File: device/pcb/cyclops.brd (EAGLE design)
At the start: 124.5 x 79.9 mm, 201 parts, among them Q1 NDS351AN, Q2 NDS351AN, Q3 NDS351AN, Q4 IRF510, U1 MCP4921, U10 LT1880, U11 ZXTD, U12 DG9421, U13 THS4281, U14 ZXTD, U16 OPA1664, U2 LT1764A, U3 BD00FC0WEFJ, U4 LTM8020, U5 LT1931, U6 TPS72325, U7 TLV3701, U75 TXB0104RGYR, U8 LT1711, U9 ADR03

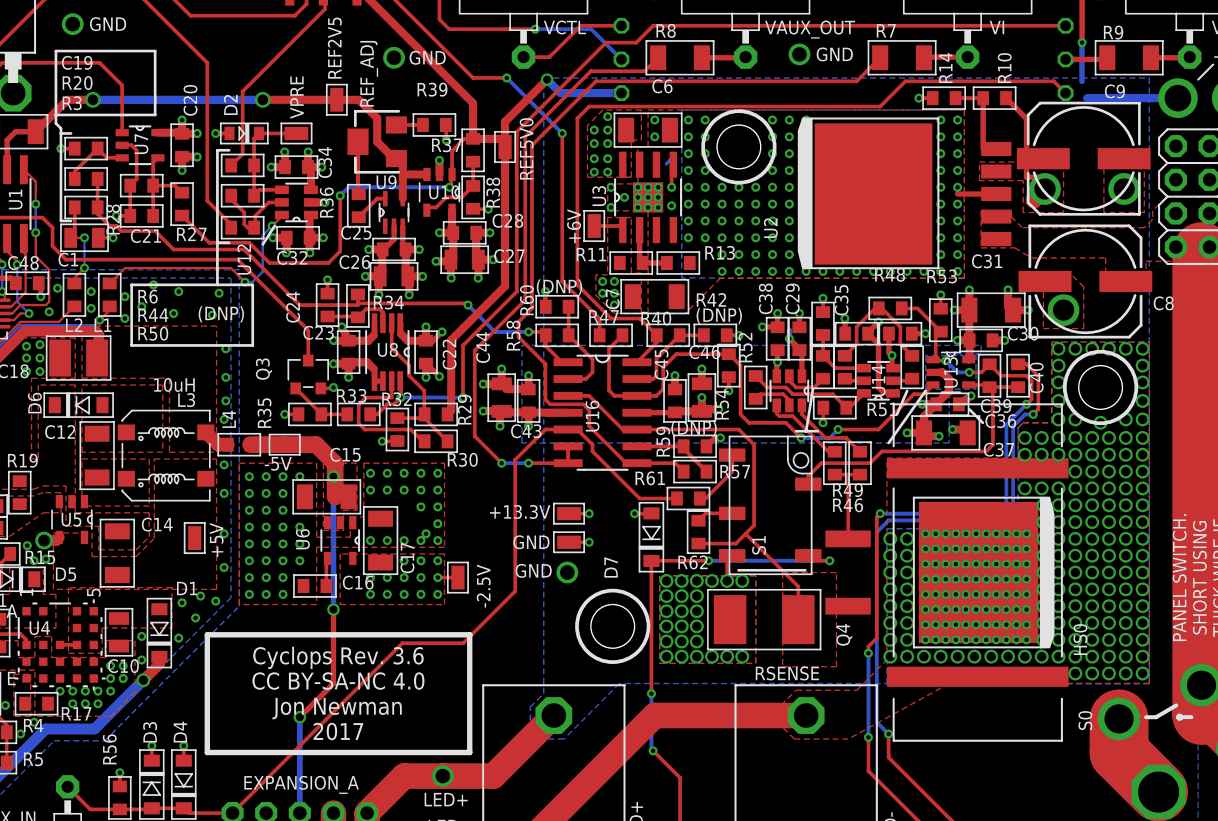
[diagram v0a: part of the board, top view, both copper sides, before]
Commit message: Ready for 3.6 production
- These designs are up to date for 3.6 production
- I need to create an assembly manual before moving forward
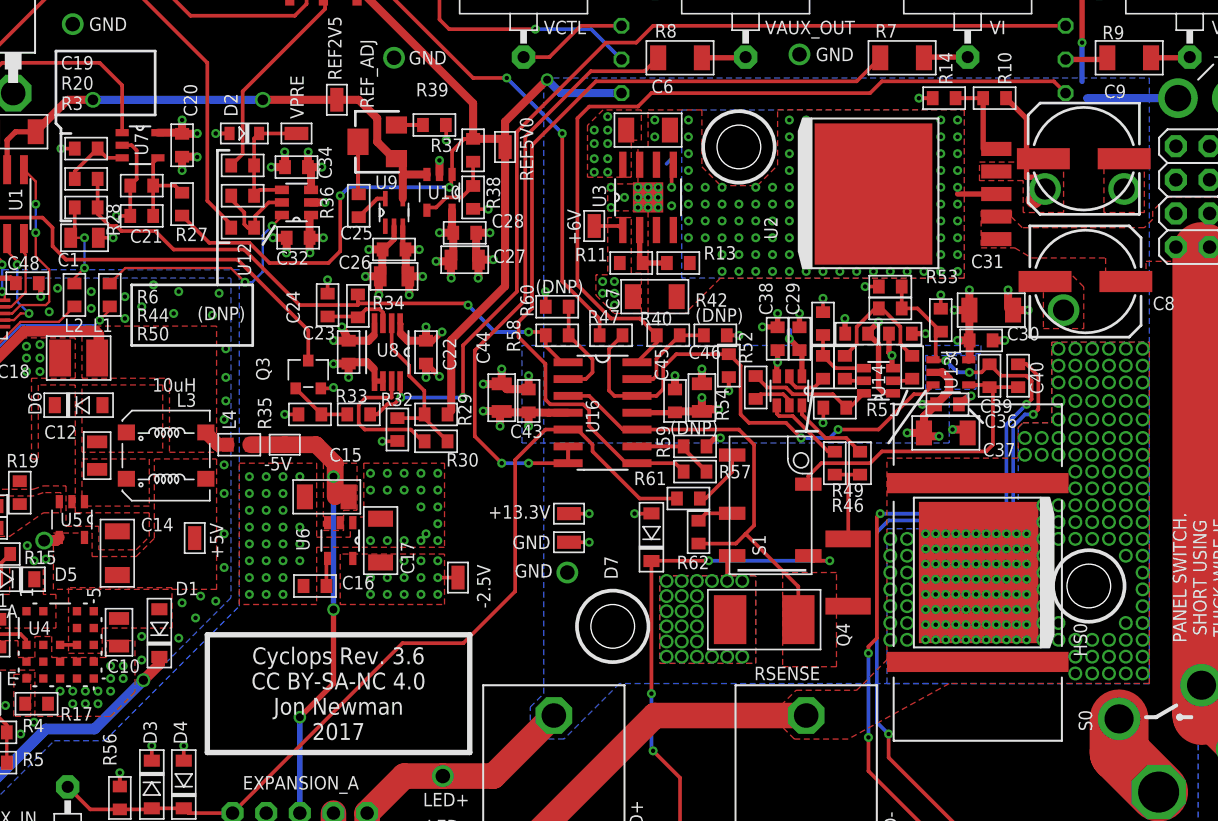
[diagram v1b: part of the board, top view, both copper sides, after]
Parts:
- added C41: 470pF, cyclops:0603
- C12: device cyclops:1206 -> jonnew:0805
- R48: value 0 -> 200
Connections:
- net GND: now also C41.2
- net N$13: now also C41.1
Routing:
- net N$13: track 66.7 -> 68.4 mm
- net GND: track 113.7 -> 114.7 mm, vias 415 -> 407
- net LED-: vias 233 -> 210

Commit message: Fixed erros found in pre-production check by Filipe.
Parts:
- R36: value 470 -> 470k
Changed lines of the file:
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@@
 <?xml version="1.0" encoding="utf-8"?>
 <!DOCTYPE eagle SYSTEM "eagle.dtd">
-<eagle version="6.5.0">
+<eagle version="6.6.0">
 <drawing>
 <settings>
@@
 <attribute name="VALUE" x="62.865" y="53.474" size="1.016" layer="27" font="vector" ratio="18"/>
 </element>
-<element name="R36" library="cyclops" package="0603" value="470" x="52.832" y="56.268" smashed="yes" rot="R270">
+<element name="R36" library="cyclops" package="0603" value="470k" x="52.832" y="56.268" smashed="yes" rot="R270">
 <attribute name="MN" value="Panasonic" x="52.832" y="53.728" size="1.778" layer="27" rot="R270" display="off"/>
 <attribute name="DK" value="PxxxxHTR-ND" x="52.832" y="53.728" size="1.778" layer="27" rot="R270" display="off"/>

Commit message: Fixed erros found in pre-production check by Filipe.
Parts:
- U12: value DG9421 -> ADG1201
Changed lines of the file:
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@@
 <attribute name="MPN" value="ERJ-3EKFxxxxV" x="52.832" y="53.728" size="1.778" layer="27" rot="R270" display="off"/>
 <attribute name="NAME" x="50.927" y="55.252" size="1.016" layer="25" font="vector" ratio="18" rot="R90"/>
-<attribute name="VALUE" x="52.07" y="55.125" size="1.016" layer="27" font="vector" ratio="18" rot="R90"/>
+<attribute name="VALUE" x="52.07" y="54.998" size="1.016" layer="27" font="vector" ratio="18" rot="R90"/>
 </element>
 <element name="R39" library="cyclops" package="0603" value="1k" x="58.547" y="62.364" smashed="yes" rot="R180">
@@
 <element name="C34" library="cyclops" package="0603" value="0.1uF" x="48.133" y="59.182" smashed="yes" rot="R180">
 <attribute name="NAME" x="50.292" y="58.293" size="1.016" layer="25" font="vector" ratio="18" rot="R270" align="center-right"/>
-<attribute name="VALUE" x="51.308" y="58.293" size="1.016" layer="27" font="vector" ratio="18" rot="R90" align="center-left"/>
+<attribute name="VALUE" x="51.308" y="58.42" size="1.016" layer="27" font="vector" ratio="18" rot="R90" align="center-left"/>
 </element>
 <element name="C32" library="cyclops" package="0603" value="0.1uF" x="48.26" y="53.848" smashed="yes" rot="R180">
@@
 <attribute name="VALUE" x="56.709" y="47.169" size="1.016" layer="27" font="vector" ratio="18" rot="SR0"/>
 </element>
-<element name="U12" library="jonnew" package="SOT23-6" value="DG9421" x="48.133" y="56.515" smashed="yes" rot="R90">
+<element name="U12" library="jonnew" package="SOT23-6" value="ADG1201" x="48.133" y="56.515" smashed="yes" rot="R90">
 <attribute name="VALUE" x="45.085" y="53.594" size="1.016" layer="27" font="vector" ratio="18" rot="R270"/>
 <attribute name="NAME" x="43.688" y="53.467" size="1.016" layer="25" font="vector" ratio="18" rot="R270"/>

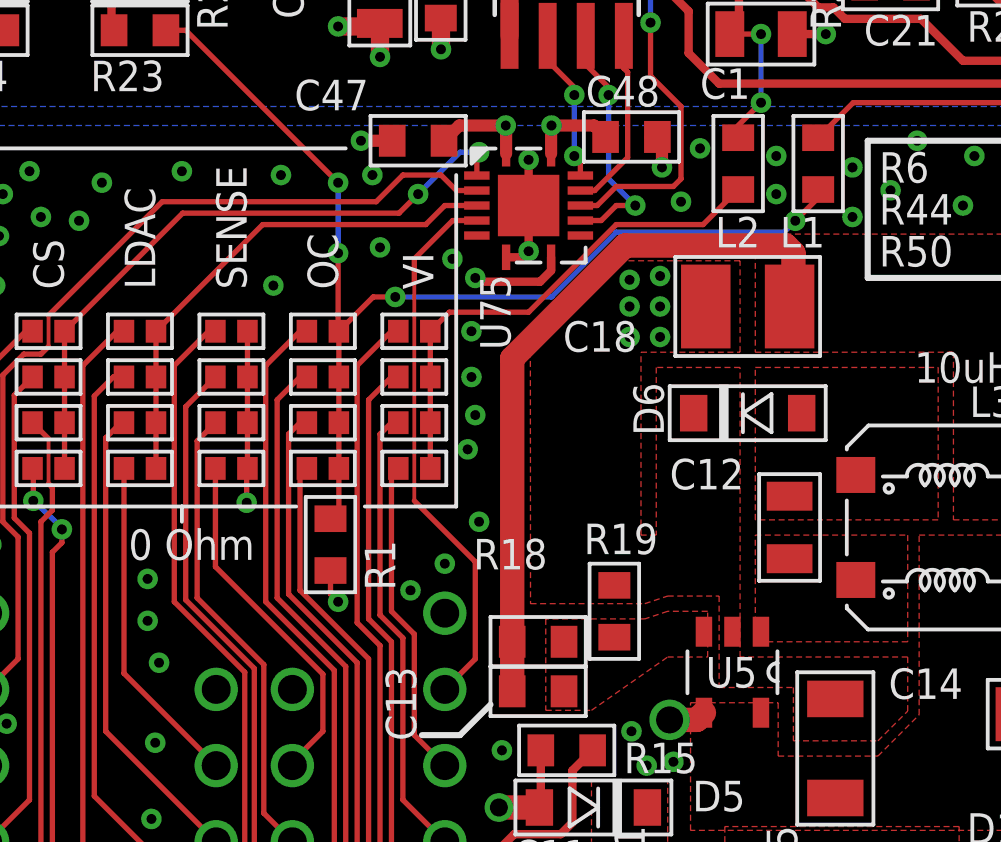
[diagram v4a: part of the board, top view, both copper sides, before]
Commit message: Simplification of cyclops library
- Also found that I had the OC and VI pins swiched on the Teensy pinout
(the OC pins were tied to A10-13 which are _only_ capable of analog
input). I simply swiched the pins and reflected that change in the
library. Now A10-13 are used for VI which is only analog in.
- For now, I will leave the GSOC dev stuff on its own branch and remove
it from the repo for the 3.6 production. Hopefully it can be integrated
in the future. It is too complicated and unfinished to be merged with
master right now.
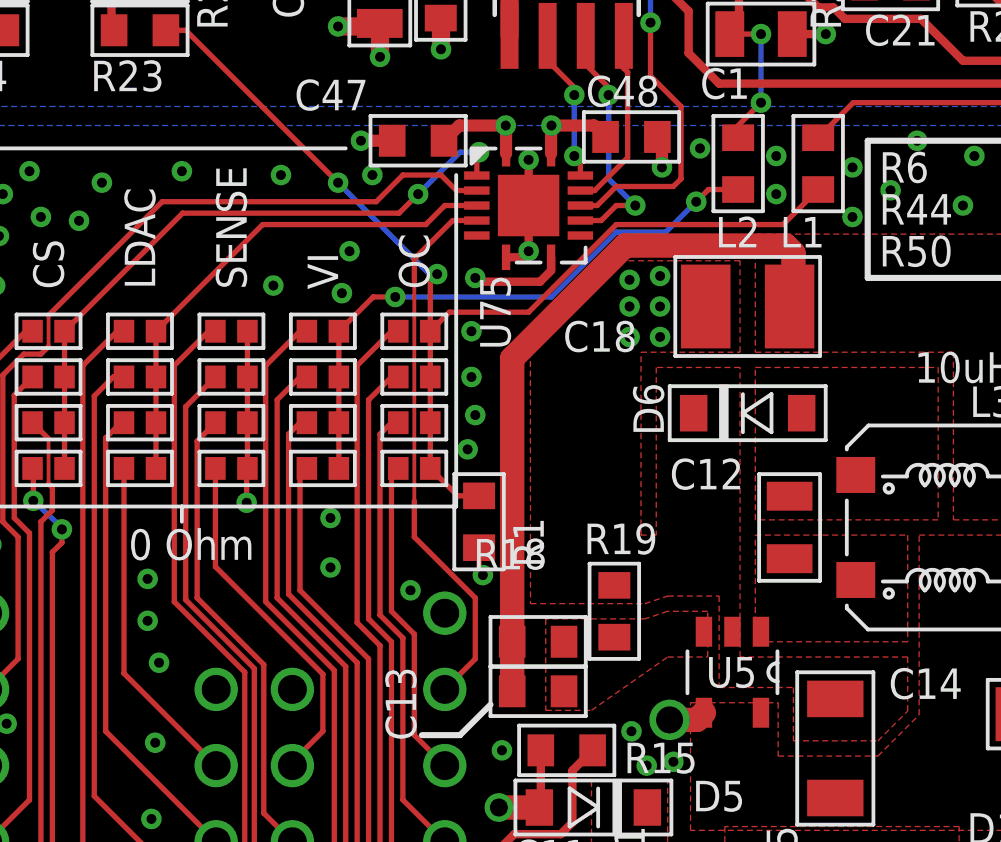
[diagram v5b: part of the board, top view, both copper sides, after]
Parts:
- moved J_VI1 5.49 mm to (17.5, 43.9), turned to 180 degrees
- moved J_VI4 5.49 mm to (17.5, 39.4), turned to 180 degrees
- moved R1 5.01 mm to (22.7, 37.6)
- moved J_LDAC1 4.57 mm to (11.4, 43.9), turned to 0 degrees
- moved J_LDAC4 4.57 mm to (11.4, 39.4), turned to 180 degrees
- moved J_OC3 3.41 mm to (20.6, 40.9), turned to 0 degrees
- moved J_OC4 3.41 mm to (20.6, 39.4), turned to 0 degrees
- moved J_VI2 3.41 mm to (17.5, 42.4), turned to 180 degrees
- moved J_VI3 3.41 mm to (17.5, 40.9), turned to 180 degrees
- moved J_OC1 3.05 mm to (20.6, 43.9), turned to 0 degrees
- moved J_OC2 3.05 mm to (20.6, 42.4), turned to 0 degrees
- moved J_CS1 1.52 mm to (8.38, 43.9)
- moved J_CS2 1.52 mm to (8.38, 42.4)
- moved J_LDAC2 1.52 mm to (11.4, 42.4)
- moved J_LDAC3 1.52 mm to (11.4, 40.9)
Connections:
- removed net N$58: J_VI1.2, J_VI2.2, J_VI3.2, J_VI4.2, L2.1
- new net VI_IN: J_VI1.1, J_VI2.1, J_VI3.1, J_VI4.1, L2.1
- net CS0: now also J_CS1.2; no longer J_CS2.2
- net CS1: now also J_CS2.2; no longer J_CS1.2
- net LDAC: now also J_LDAC1.2, J_LDAC4.1; no longer J_LDAC1.1, J_LDAC4.2
- net LDAC0: now also J_LDAC1.1; no longer J_LDAC4.1
- net LDAC1: now also J_LDAC2.2; no longer J_LDAC3.2
- net LDAC2: now also J_LDAC3.2; no longer J_LDAC2.2
- net LDAC3: now also J_LDAC4.2; no longer J_LDAC1.2
- net VI0: now also J_VI1.2, UC.A13; no longer J_VI4.1, UC.22/A8
- net VI1: now also J_VI2.2, UC.A12; no longer J_VI3.1, UC.17/A3
- net VI2: now also J_VI3.2, UC.A10; no longer J_VI2.1, UC.16/A2
- net VI3: now also J_VI4.2, UC.A11; no longer J_VI1.1, UC.15/A1
- net ~OC0: now also J_OC1.1, UC.22/A8; no longer J_OC1.2, UC.A13
- net ~OC1: now also J_OC2.1, UC.17/A3; no longer J_OC2.2, UC.A12
- net ~OC2: now also J_OC3.1, UC.16/A2; no longer J_OC3.2, UC.A11
- net ~OC3: now also J_OC4.1, UC.15/A1; no longer J_OC4.2, UC.A10
- net ~OVER_CURR_PRE: now also J_OC1.2, J_OC2.2, J_OC3.2, J_OC4.2; no longer J_OC1.1, J_OC2.1, J_OC3.1, J_OC4.1
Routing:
- net ~OC3: track 31.6 -> 10.7 mm
- net VI_IN: track 0.00 -> 19.8 mm, vias 0 -> 2
- net N$58: track 16.9 -> 0.00 mm
- net VI2: track 15.3 -> 31.6 mm
- net VI3: track 10.7 -> 26.2 mm
- net ~OC1: track 33.6 -> 19.6 mm
- net VI1: track 19.6 -> 33.6 mm
- net ~OC2: track 26.2 -> 15.3 mm
- net ~OC0: track 29.4 -> 34.2 mm
- net VI0: track 34.2 -> 29.4 mm
- net ~OVER_CURR_PRE: track 37.3 -> 35.9 mm, vias 4 -> 2
- net +3V3: track 58.5 -> 59.8 mm
- net GND: vias 407 -> 406

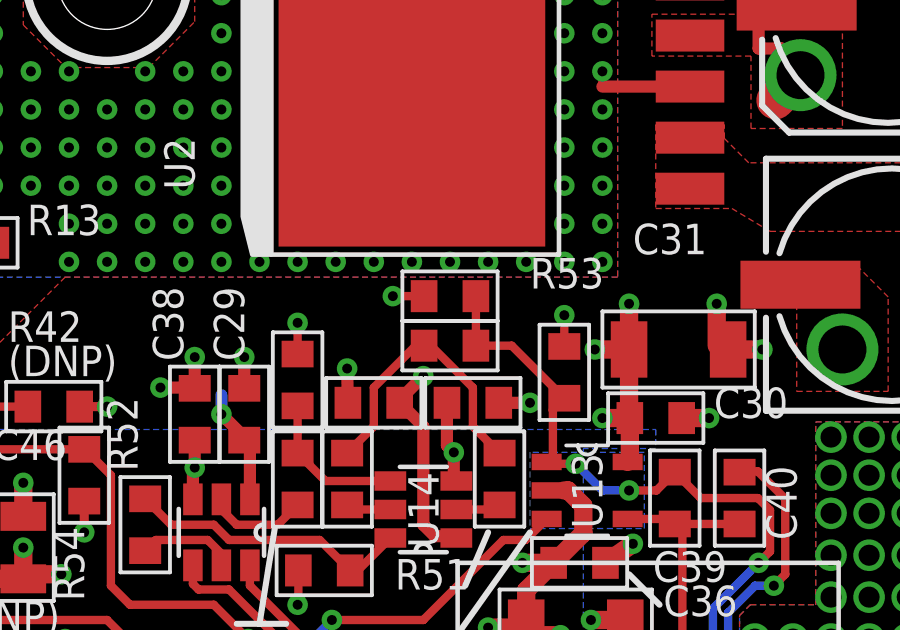
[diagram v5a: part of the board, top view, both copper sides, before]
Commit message: Compensation capacitor to silince ringing in BJT booster stage
- Seems to cure all ringing for different LEDs and cable lengths
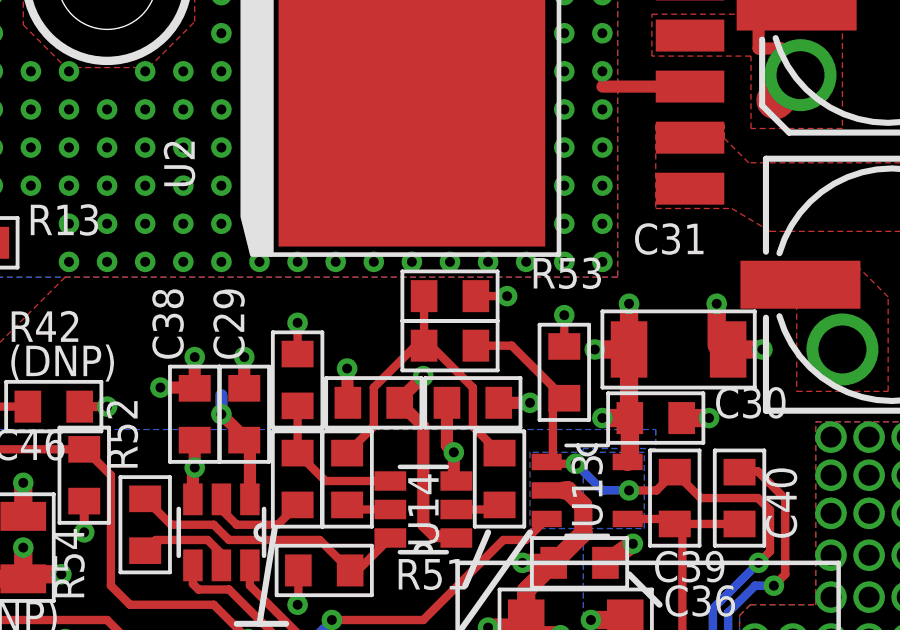
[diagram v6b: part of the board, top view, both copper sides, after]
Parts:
- C41: value 470pF -> 24pF
- R53: value 1k -> 470
- turned C41 to 0 degrees
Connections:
- removed net N$16: R45.1, R48.2, R51.1
- new net N$58: C41.1, R45.1, R48.2, R51.1
- net N$13: no longer C41.1
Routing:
- net N$58: track 0.00 -> 11.2 mm
- net N$16: track 9.56 -> 0.00 mm
- net N$13: track 68.4 -> 66.7 mm
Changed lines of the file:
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@@
 <text x="58.42" y="3.175" size="1.016" layer="22" font="vector" ratio="18" rot="MR0" align="center">SCL</text>
 <text x="60.96" y="5.08" size="1.016" layer="22" font="vector" ratio="18" rot="MR0" align="center">SDA</text>
-<text x="42.672" y="77.089" size="1.016" layer="22" font="vector" ratio="18" rot="MR0">DAC&lt;OFF&gt;VCTL</text>
+<text x="27.432" y="74.676" size="1.016" layer="22" font="vector" ratio="18" rot="MR0">DAC&lt;OFF&gt;VCTL</text>
 <text x="8.382" y="45.339" size="1.016" layer="21" font="vector" ratio="18" rot="R90" align="center-left">CS</text>
 <text x="11.43" y="45.339" size="1.016" layer="21" font="vector" ratio="18" rot="R90" align="center-left">LDAC</text>
@@
 <attribute name="VALUE" x="93.218" y="39.751" size="1.016" layer="27" font="vector" ratio="18" rot="R180" align="center-left"/>
 </element>
-<element name="R53" library="cyclops" package="0603" value="1k" x="96.774" y="47.625" smashed="yes" rot="R270">
+<element name="R53" library="cyclops" package="0603" value="470" x="96.774" y="47.625" smashed="yes" rot="R270">
 <attribute name="MN" value="Panasonic" x="96.774" y="47.625" size="1.778" layer="27" rot="R270" display="off"/>
 <attribute name="DK" value="PxxxxHTR-ND" x="96.774" y="47.625" size="1.778" layer="27" rot="R270" display="off"/>
 <attribute name="MPN" value="ERJ-3EKFxxxxV" x="96.774" y="47.625" size="1.778" layer="27" rot="R270" display="off"/>
 <attribute name="NAME" x="95.631" y="50.927" size="1.016" layer="25" font="vector" ratio="18" rot="R180" align="center-right"/>
-<attribute name="VALUE" x="96.012" y="49.911" size="1.016" layer="27" font="vector" ratio="18" align="center-left"/>
+<attribute name="VALUE" x="95.758" y="49.911" size="1.016" layer="27" font="vector" ratio="18" align="center-left"/>
 </element>
 <element name="C29" library="jonnew" package="0603" value=".1uF" x="86.106" y="46.228" smashed="yes" rot="R90">
@@
 <attribute name="VALUE" x="73.787" y="28.067" size="1.016" layer="27" font="vector" ratio="18" rot="R90"/>
 </element>
-<element name="C41" library="cyclops" package="0603" value="470pF" x="92.964" y="50.165" smashed="yes" rot="R180">
-<attribute name="VALUE" x="91.948" y="50.8" size="1.016" layer="27" font="vector" ratio="18" rot="R180" align="center-left"/>
+<element name="C41" library="cyclops" package="0603" value="24pF" x="92.964" y="50.165" smashed="yes">
+<attribute name="VALUE" x="91.567" y="50.927" size="1.016" layer="27" font="vector" ratio="18" rot="R180" align="center-left"/>
 </element>
 </elements>
@@
 <wire x1="24.183" y1="46.408" x2="24.384" y2="46.609" width="0.2794" layer="1"/>
 <contactref element="C41" pad="2"/>
-<via x="91.059" y="50.165" extent="1-16" drill="0.3302"/>
-<wire x1="91.059" y1="50.165" x2="92.1004" y2="50.165" width="0.2794" layer="1"/>
+<via x="94.869" y="50.165" extent="1-16" drill="0.3302"/>
+<wire x1="94.869" y1="50.165" x2="93.8276" y2="50.165" width="0.2794" layer="1"/>
 <via x="17.78" y="36.068" extent="1-16" drill="0.3302"/>
 </signal>
@@
 <via x="91.313" y="22.479" extent="1-16" drill="0.3302"/>
 <wire x1="91.313" y1="22.479" x2="91.313" y2="16.129" width="0.2794" layer="16"/>
-<contactref element="C41" pad="1"/>
-<wire x1="93.8276" y1="48.514" x2="93.8276" y2="50.165" width="0.2794" layer="1"/>
 </signal>
 <signal name="N$24">
@@
 <wire x1="86.021" y1="27.517" x2="82.042" y2="31.496" width="0.2794" layer="1"/>
 </signal>
-<signal name="N$16">
-<contactref element="R48" pad="2"/>
-<contactref element="R45" pad="1"/>
-<contactref element="R51" pad="1"/>
-<wire x1="92.1004" y1="48.514" x2="92.329" y2="48.514" width="0.2794" layer="1"/>
-<wire x1="92.329" y1="48.514" x2="93.726" y2="47.117" width="0.2794" layer="1"/>
-<wire x1="93.726" y1="47.117" x2="93.726" y2="45.8216" width="0.2794" layer="1"/>
-<wire x1="93.726" y1="45.8216" x2="94.615" y2="44.9326" width="0.2794" layer="1"/>
-<wire x1="92.1004" y1="48.514" x2="91.821" y2="48.514" width="0.2794" layer="1"/>
-<wire x1="91.821" y1="48.514" x2="90.424" y2="47.117" width="0.2794" layer="1"/>
-<wire x1="90.424" y1="47.117" x2="90.424" y2="45.8216" width="0.2794" layer="1"/>
-<wire x1="90.424" y1="45.8216" x2="89.535" y2="44.9326" width="0.2794" layer="1"/>
-</signal>
 <signal name="N$40">
 <contactref element="C40" pad="2"/>
@@
 <wire x1="30.3784" y1="48.6664" x2="31.369" y2="48.6664" width="0.1778" layer="1"/>
 </signal>
+<signal name="N$58">
+<contactref element="C41" pad="1"/>
+<contactref element="R48" pad="2"/>
+<contactref element="R45" pad="1"/>
+<contactref element="R51" pad="1"/>
+<wire x1="92.1004" y1="48.514" x2="92.329" y2="48.514" width="0.2794" layer="1"/>
+<wire x1="92.329" y1="48.514" x2="93.726" y2="47.117" width="0.2794" layer="1"/>
+<wire x1="93.726" y1="47.117" x2="93.726" y2="45.8216" width="0.2794" layer="1"/>
+<wire x1="93.726" y1="45.8216" x2="94.615" y2="44.9326" width="0.2794" layer="1"/>
+<wire x1="92.1004" y1="48.514" x2="91.821" y2="48.514" width="0.2794" layer="1"/>
+<wire x1="91.821" y1="48.514" x2="90.424" y2="47.117" width="0.2794" layer="1"/>
+<wire x1="90.424" y1="47.117" x2="90.424" y2="45.8216" width="0.2794" layer="1"/>
+<wire x1="90.424" y1="45.8216" x2="89.535" y2="44.9326" width="0.2794" layer="1"/>
+<wire x1="92.1004" y1="50.165" x2="92.1004" y2="48.514" width="0.2794" layer="1"/>
+</signal>
 </signals>
